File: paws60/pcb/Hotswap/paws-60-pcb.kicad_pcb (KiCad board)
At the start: 2 copper layers, 284.7 x 94.2 mm, 160 parts, among them J1 JST SH 4-pin, J2 AVR-ISP-6, SW1 Reset, U1 SRV05-4, U2 ATmega32U4-AU, Y1 16MHz

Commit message: Updated PCB for Paws60, remove ISO layout
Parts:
- removed the D45 at (38.7, 71.9)
- removed the MX44 at (251.9, 47.1)
- removed the MX46 at (273.3, 37.6)
- removed the MX47 at (11.4, 66.2)
- removed the MX49 at (32.8, 66.2)
- MX30: footprint MX_Only:MXOnly-1.5U-Hotswap-Rotated -> MX_Only:MXOnly-1.5U-Hotswap
- MX44: renamed from MX45; footprint MX_Only:MXOnly-2.25U-Hotswap-ReversedStabilizers-Left -> MX_Only:MXOnly-2.25U-Hotswap
- MX58: renamed from MX62; footprint MX_Only:MXOnly-2.75U-Hotswap -> MX_Only:MXOnly-2.75U-Hotswap-ReversedStabilizers
- moved D1 15.4 mm to (2.64, 3.98)
- moved D43 5.22 mm to (4.19, 67.3)
- moved J2 3.94 mm to (3.07, 20.3)
- moved R2 3.59 mm to (35.9, 16.4)
- moved C5 3.32 mm to (44.0, 32.3)
- moved Y1 3.30 mm to (44.0, 35.0)
- moved C7 3.28 mm to (44.0, 37.7)
- moved D42 2.52 mm to (244.9, 49.2)
- moved R1 2.32 mm to (34.7, 18.7)
- moved C2 2.29 mm to (14.9, 38.2)
- moved C4 2.23 mm to (21.8, 26.9)
- moved D3 1.91 mm to (36.8, 6.88)
- moved U2 1.77 mm to (26.8, 37.7)
- moved U1 1.73 mm to (40.1, 17.5)
- moved D2 0.74 mm to (19.6, 9.79)
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- renumbered D43 to D42, D44 to D43, D46 to D44, D47 to D45, D48 to D46, D49 to D47, D50 to D48, D51 to D49, D52 to D50, D53 to D51, D54 to D52, D55 to D53, D56 to D54, D57 to D55, D58 to D56, D59 to D57, D60 to D58, D61 to D59, D62 to D60, D63 to D61, D64 to D62, D65 to D63, MX48 to MX45, MX50 to MX46, MX51 to MX47, MX52 to MX48, MX53 to MX49, MX54 to MX50, MX55 to MX51, MX56 to MX52, MX57 to MX53, MX58 to MX54, MX59 to MX55, MX60 to MX56, MX61 to MX57, MX63 to MX59, MX64 to MX60, MX65 to MX61, MX66 to MX62, MX67 to MX63, MX68 to MX64, MX69 to MX65, MX70 to MX66, MX71 to MX67, MX72 to MX68, MX73 to MX69, MX74 to MX70, MX75 to MX71, MX76 to MX72, MX77 to MX73
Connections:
- D42 pad 2: Net-(D43-Pad2) (its old number) -> Net-(D42-Pad2)
- MX44 pad 1: Net-(D43-Pad2) (its old number) -> Net-(D42-Pad2)
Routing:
- net COL4: track 225.5 -> 298.4 mm, vias 5 -> 10
- net COL5: track 282.8 -> 350.6 mm, vias 5 -> 10
- net COL3: track 186.0 -> 245.5 mm, vias 5 -> 7
- net Net-(D43-Pad2): track 61.2 -> 10.5 mm
- net COL6: track 412.0 -> 459.1 mm, vias 9 -> 13
- net ROW2: track 349.0 -> 396.0 mm, vias 4 -> 6
- net Net-(D45-Pad2) (its old number): track 41.3 -> 0.00 mm, vias 4 -> 0
- net Net-(D42-Pad2): track 11.9 -> 48.2 mm
- net Net-(D43-Pad2) (its old number): track 30.2 -> 0.00 mm
- net COL7: track 396.2 -> 425.5 mm, vias 5 -> 10
- net ROW0: track 339.3 -> 366.4 mm
- net +5V: track 119.6 -> 142.6 mm, vias 6 -> 7
- net Net-(D2-Pad2): track 3.01 -> 20.6 mm
- net COL2: track 209.2 -> 226.5 mm, vias 13 -> 12
- net COL13: track 456.7 -> 440.6 mm, vias 12 -> 11
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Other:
- outline, holes or cut-outs redrawn

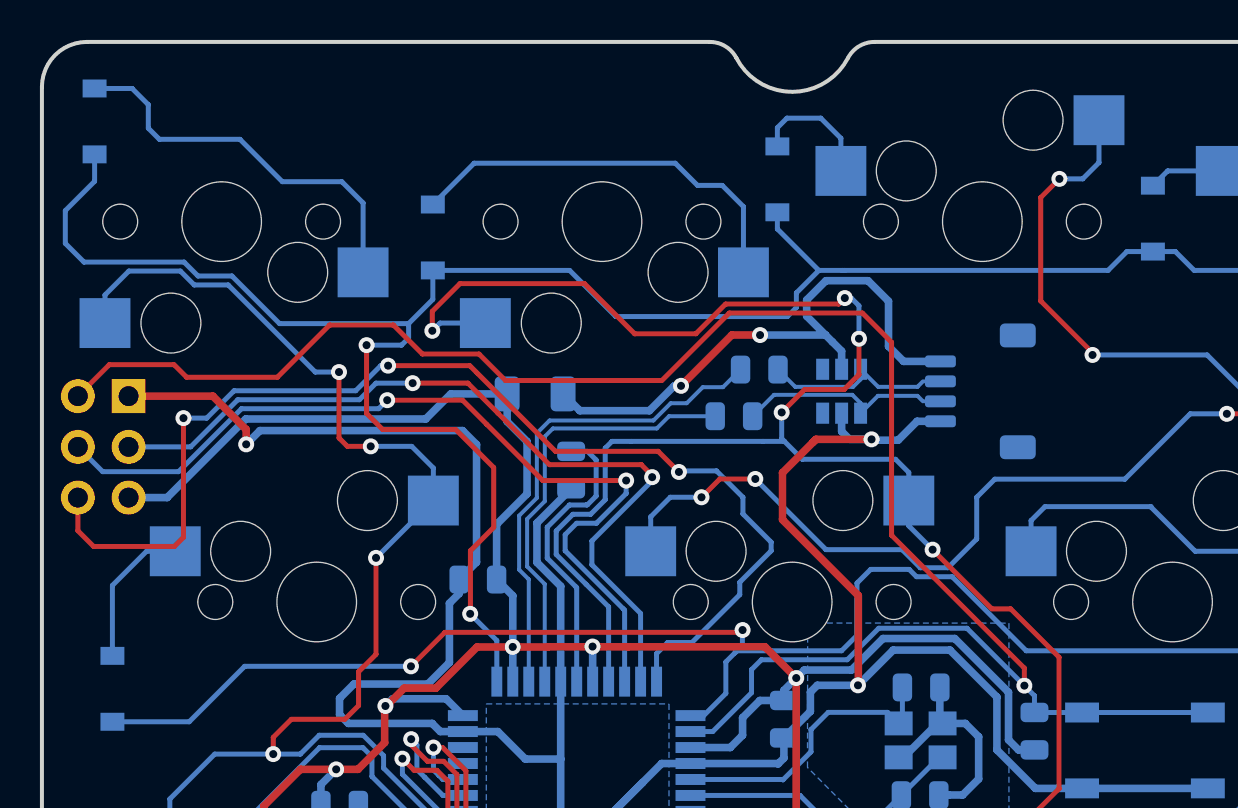
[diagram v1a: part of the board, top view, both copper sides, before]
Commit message: Added USB-C port, still not sure it correct or not
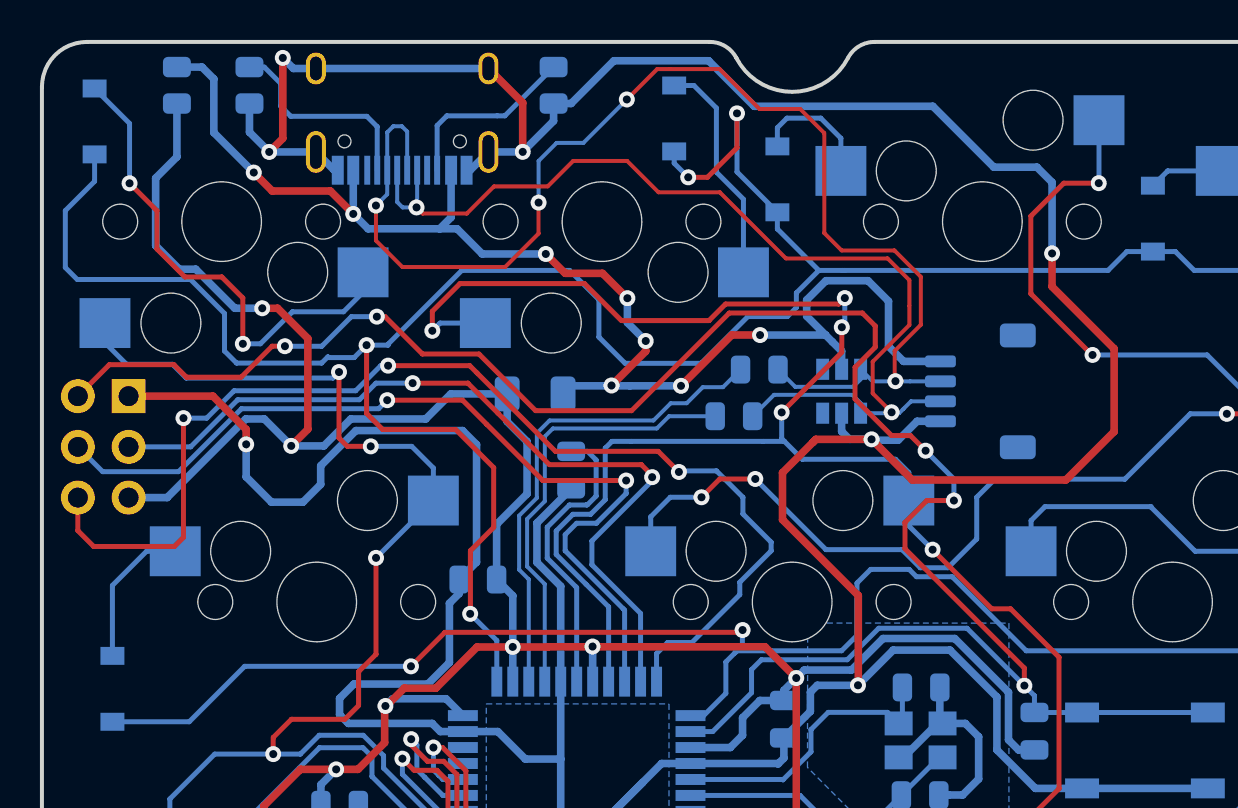
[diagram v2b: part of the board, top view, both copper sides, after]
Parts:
- added F2: Polyfuse, Resistor_SMD:R_0805_2012Metric, B.Cu at (6.76, 2.17)
- added R5: 5.1k, Resistor_SMD:R_0805_2012Metric, B.Cu at (10.4, 2.17)
- added R6: 5.1k, Resistor_SMD:R_0805_2012Metric, B.Cu at (25.6, 2.17)
- added USB1: HRO-TYPE-C-31-M-12, Type-C:HRO-TYPE-C-31-M-12, B.Cu at (18.0, -1.27)
- moved D2 13.5 mm to (31.7, 3.83)
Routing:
- net GND: track 181.1 -> 274.4 mm, vias 5 -> 9
- net D-: track 9.63 -> 65.3 mm, vias 0 -> 4
- net D+: track 11.0 -> 51.5 mm, vias 0 -> 2
- net VBUS: track 29.4 -> 68.4 mm, vias 2 -> 8
- net +5V: track 142.6 -> 166.6 mm, vias 7 -> 9
- net ROW0: track 366.4 -> 381.2 mm, vias 6 -> 8
- net Net-(R5-Pad1): track 0.00 -> 10.5 mm
- net Net-(R6-Pad1): track 0.00 -> 9.28 mm
- net Net-(D2-Pad2): track 20.6 -> 11.4 mm
- net RST: track 96.8 -> 102.7 mm, vias 1 -> 5
- net Net-(D1-Pad2): track 20.0 -> 25.0 mm, vias 0 -> 2
- net COL1: track 205.6 -> 203.2 mm
- net COL0: track 199.7 -> 197.5 mm
- net COL2: track 226.5 -> 227.2 mm
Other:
- board text added: "Paws 60 v1.0"
- board text removed: "Bakeneko 60 v3.0"

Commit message: Move crystal more closer to MCU, ya yeet
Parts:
- moved Y1 5.39 mm to (38.8, 36.5)
- moved C5 5.39 mm to (38.9, 33.8)
- moved C7 5.35 mm to (38.8, 39.2)
- moved C1 1.56 mm to (35.6, 33.7)
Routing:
- net XTAL2: track 14.6 -> 7.71 mm
- net XTAL1: track 14.5 -> 8.83 mm
- net Net-(D17-Pad2): track 48.9 -> 47.6 mm
- net RST: track 102.7 -> 103.5 mm
- net +5V: track 166.6 -> 167.3 mm
- net GND: track 274.4 -> 274.0 mm, vias 9 -> 11

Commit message: Re-wire, ...
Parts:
- removed the D42 at (244.9, 49.2)
- MX58: footprint MX_Only:MXOnly-2.75U-Hotswap-ReversedStabilizers -> MX_Only:MXOnly-2.75U-Hotswap
- moved D20 13.9 mm to (86.3, 16.1)
- moved D55 10.6 mm to (282.5, 61.0)
- moved D29 2.60 mm to (258.6, 28.8)
- moved D63 1.52 mm to (261.3, 87.5)
- moved D62 1.38 mm to (237.5, 87.4)
- moved D17 0.67 mm to (67.3, 16.1)
- moved F1 0.54 mm to (24.2, 17.6)
- moved C6 0.46 mm to (26.0, 21.4)
- moved C5 0.43 mm to (38.9, 33.4)
- moved Y1 0.42 mm to (38.8, 36.1)
- moved C7 0.38 mm to (38.8, 38.8)
- turned MX56 to 180 degrees
- turned MX57 to 180 degrees
- turned MX58 to 0 degrees
- turned MX64 to 180 degrees
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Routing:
- net COL13: track 440.6 -> 402.0 mm, vias 11 -> 8
- net Net-(D55-Pad2): track 22.3 -> 47.9 mm
- net ROW3: track 353.0 -> 374.9 mm, vias 4 -> 6
- net Net-(D42-Pad2): track 48.2 -> 30.4 mm
- net ROW2: track 396.0 -> 379.9 mm, vias 6 -> 4
- net Net-(D54-Pad2): track 6.96 -> 22.1 mm
- net Net-(D20-Pad2): track 3.17 -> 15.2 mm, vias 0 -> 2
- net ROW1: track 324.4 -> 314.7 mm, vias 2 -> 4
- net ROW4: track 374.4 -> 365.2 mm
- net COL3: track 245.5 -> 236.3 mm
- net COL1: track 203.2 -> 195.1 mm, vias 12 -> 10
- net GND: track 274.0 -> 266.1 mm
- net ROW0: track 381.2 -> 374.9 mm
- net COL4: track 298.4 -> 292.2 mm
- net COL5: track 350.6 -> 344.6 mm
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
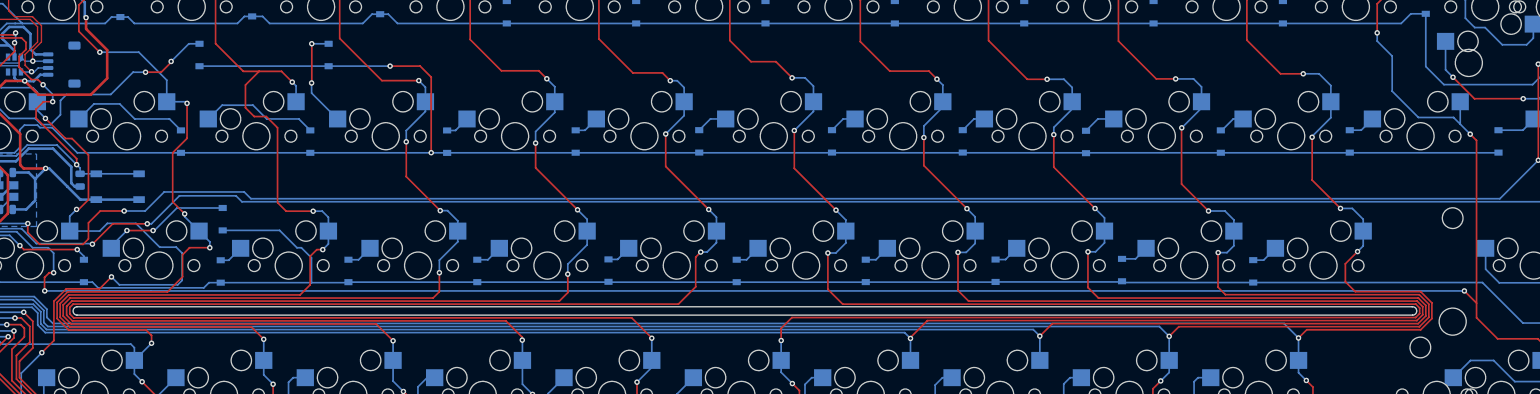
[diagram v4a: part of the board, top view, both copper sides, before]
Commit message: Move diode out, since it was accident block JST port
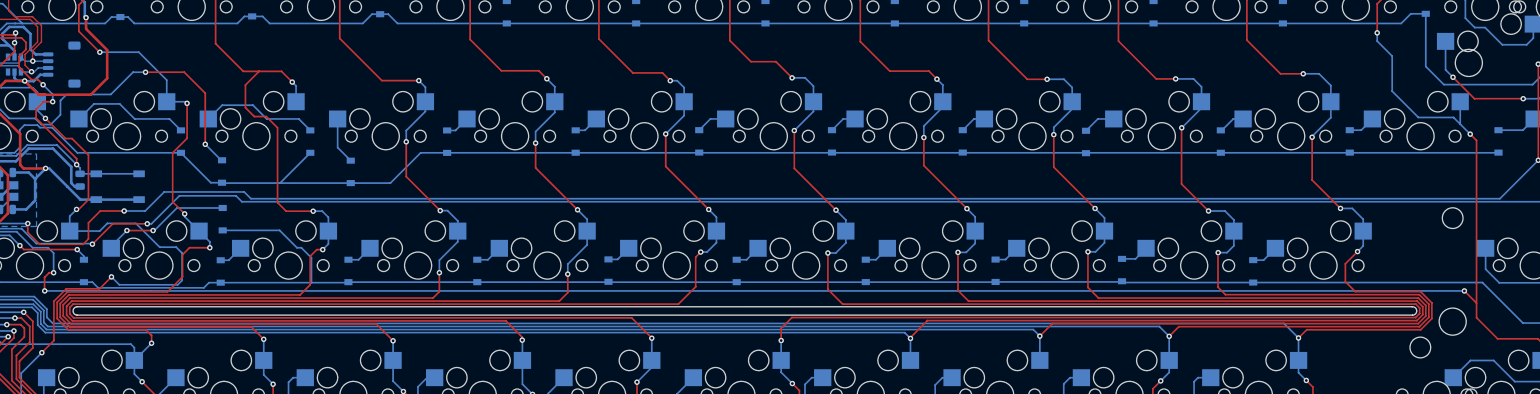
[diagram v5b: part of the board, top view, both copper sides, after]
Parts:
- moved D20 17.5 mm to (89.6, 33.3)
- moved D17 17.5 mm to (70.6, 33.2)
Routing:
- net ROW1: track 314.7 -> 278.7 mm, vias 4 -> 2
- net Net-(D17-Pad2): track 47.3 -> 58.7 mm
- net Net-(D20-Pad2): track 15.2 -> 6.94 mm, vias 2 -> 0
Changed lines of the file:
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@@
   )
   (footprint "Diode_SMD:D_SOD-123" (layer "B.Cu")
-    (at 67.290028 16.087692 90)
+    (at 70.614414 33.244321 90)
     (descr "SOD-123")
     (tags "SOD-123")
@@
   )
   (footprint "Diode_SMD:D_SOD-123" (layer "B.Cu")
-    (at 86.309883 16.087692 90)
+    (at 89.572531 33.301911 90)
     (descr "SOD-123")
     (tags "SOD-123")
@@
   (segment (start 3.530355 27.220074) (end 3.530355 30.749098) (width 0.25) (layer "B.Cu") (net 20))
   (segment (start 6.6775 25.51) (end 5.240429 25.51) (width 0.25) (layer "B.Cu") (net 20))
-  (segment (start 59.346744 18.625704) (end 61.656169 18.625704) (width 0.25) (layer "F.Cu") (net 21))
+  (segment (start 65.056628 18.625704) (end 68.142143 21.711219) (width 0.25) (layer "F.Cu") (net 21))
   (segment (start 33.033815 22.804311) (end 33.95009 21.888036) (width 0.25) (layer "F.Cu") (net 21))
-  (segment (start 61.656169 18.625704) (end 63.152415 17.129458) (width 0.25) (layer "F.Cu") (net 21))
+  (segment (start 59.346744 18.625704) (end 65.056628 18.625704) (width 0.25) (layer "F.Cu") (net 21))
+  (segment (start 68.142143 21.711219) (end 68.142143 29.236315) (width 0.25) (layer "F.Cu") (net 21))
   (segment (start 33.95009 21.888036) (end 35.728742 21.888036) (width 0.25) (layer "F.Cu") (net 21))
   (via (at 35.728742 21.888036) (size 0.8) (drill 0.4) (layers "F.Cu" "B.Cu") (net 21))
+  (via (at 68.142143 29.236315) (size 0.8) (drill 0.4) (layers "F.Cu" "B.Cu") (net 21))
   (via (at 33.033815 22.804311) (size 0.8) (drill 0.4) (layers "F.Cu" "B.Cu") (net 21))
   (via (at 59.346744 18.625704) (size 0.8) (drill 0.4) (layers "F.Cu" "B.Cu") (net 21))
-  (via (at 63.117264 17.03842) (size 0.8) (drill 0.4) (layers "F.Cu" "B.Cu") (net 21))
   (segment (start 54.237506 21.898925) (end 57.510727 18.625704) (width 0.25) (layer "B.Cu") (net 21))
   (segment (start 35.728742 21.888036) (end 39.268713 25.428007) (width 0.25) (layer "B.Cu") (net 21))
   (segment (start 43.081174 25.428007) (end 43.987833 26.334666) (width 0.25) (layer "B.Cu") (net 21))
   (segment (start 30.49 25.51) (end 30.49 23.785068) (width 0.25) (layer "B.Cu") (net 21))
+  (segment (start 70.500149 31.594321) (end 68.142143 29.236315) (width 0.25) (layer "B.Cu") (net 21))
   (segment (start 31.470757 22.804311) (end 33.033815 22.804311) (width 0.25) (layer "B.Cu") (net 21))
   (segment (start 30.49 23.785068) (end 31.470757 22.804311) (width 0.25) (layer "B.Cu") (net 21))
   (segment (start 39.268713 25.428007) (end 43.081174 25.428007) (width 0.25) (layer "B.Cu") (net 21))
-  (segment (start 67.290028 14.437692) (end 65.717992 14.437692) (width 0.25) (layer "B.Cu") (net 21))
+  (segment (start 70.614414 31.594321) (end 70.500149 31.594321) (width 0.25) (layer "B.Cu") (net 21))
   (segment (start 47.722677 21.898925) (end 54.237506 21.898925) (width 0.25) (layer "B.Cu") (net 21))
-  (segment (start 65.717992 14.437692) (end 63.117264 17.03842) (width 0.25) (layer "B.Cu") (net 21))
   (segment (start 46.817291 22.804311) (end 47.722677 21.898925) (width 0.25) (layer "B.Cu") (net 21))
   (segment (start 43.987833 26.334666) (end 45.376583 26.334666) (width 0.25) (layer "B.Cu") (net 21))
@@
   (segment (start 46.817291 24.893958) (end 46.817291 22.804311) (width 0.25) (layer "B.Cu") (net 21))
   (segment (start 45.376583 26.334666) (end 46.817291 24.893958) (width 0.25) (layer "B.Cu") (net 21))
-  (segment (start 99.798033 17.724283) (end 95.365912 17.724283) (width 0.25) (layer "F.Cu") (net 22))
   (segment (start 20.184579 29.57) (end 34.976335 29.57) (width 0.25) (layer "F.Cu") (net 22))
-  (segment (start 101.421837 30.48) (end 101.421837 19.348087) (width 0.25) (layer "F.Cu") (net 22))
-  (segment (start 101.421837 19.348087) (end 99.798033 17.724283) (width 0.25) (layer "F.Cu") (net 22))
   (segment (start 34.976335 29.57) (end 35.091728 29.454607) (width 0.25) (layer "F.Cu") (net 22))
   (segment (start 18.48296 31.271619) (end 20.184579 29.57) (width 0.25) (layer "F.Cu") (net 22))
   (via (at 35.091728 29.454607) (size 0.8) (drill 0.4) (layers "F.Cu" "B.Cu") (net 22))
   (via (at 18.48296 31.271619) (size 0.8) (drill 0.4) (layers "F.Cu" "B.Cu") (net 22))
-  (via (at 101.421837 30.48) (size 0.8) (drill 0.4) (layers "F.Cu" "B.Cu") (net 22))
-  (via (at 95.365912 17.724283) (size 0.8) (drill 0.4) (layers "F.Cu" "B.Cu") (net 22))
   (segment (start 3.530355 34.049098) (end 7.377436 34.049098) (width 0.25) (layer "B.Cu") (net 22))
   (segment (start 43.801636 26.784186) (end 43.434954 26.417505) (width 0.25) (layer "B.Cu") (net 22))
   (segment (start 40.821567 29.722973) (end 40.05079 30.49375) (width 0.25) (layer "B.Cu") (net 22))
   (segment (start 10.154915 31.271619) (end 10.139034 31.2875) (width 0.25) (layer "B.Cu") (net 22))
+  (segment (start 89.572531 34.951911) (end 70.672004 34.951911) (width 0.25) (layer "B.Cu") (net 22))
   (segment (start 32.482533 33.739519) (end 32.482533 31.282609) (width 0.25) (layer "B.Cu") (net 22))
   (segment (start 18.48296 31.271619) (end 10.154915 31.271619) (width 0.25) (layer "B.Cu") (net 22))
+  (segment (start 79.211929 34.894321) (end 83.6125 30.49375) (width 0.25) (layer "B.Cu") (net 22))
+  (segment (start 68.963071 34.894321) (end 64.5625 30.49375) (width 0.25) (layer "B.Cu") (net 22))
   (segment (start 45.588288 26.784186) (end 43.801636 26.784186) (width 0.25) (layer "B.Cu") (net 22))
-  (segment (start 67.28452 17.724283) (end 95.365912 17.724283) (width 0.25) (layer "B.Cu") (net 22))
+  (segment (start 258.59 30.49375) (end 99.8675 30.49375) (width 0.25) (layer "B.Cu") (net 22))
   (segment (start 32.482533 31.282609) (end 33.271392 30.49375) (width 0.25) (layer "B.Cu") (net 22))
   (segment (start 43.434954 26.417505) (end 41.506682 26.417505) (width 0.25) (layer "B.Cu") (net 22))
+  (segment (start 70.672004 34.951911) (end 70.614414 34.894321) (width 0.25) (layer "B.Cu") (net 22))
+  (segment (start 70.614414 34.894321) (end 68.963071 34.894321) (width 0.25) (layer "B.Cu") (net 22))
   (segment (start 7.377436 34.049098) (end 10.139034 31.2875) (width 0.25) (layer "B.Cu") (net 22))
   (segment (start 40.821567 27.10262) (end 40.821567 29.722973) (width 0.25) (layer "B.Cu") (net 22))
   (segment (start 33.271392 30.49375) (end 40.05079 30.49375) (width 0.25) (layer "B.Cu") (net 22))
+  (segment (start 95.409339 34.951911) (end 89.572531 34.951911) (width 0.25) (layer "B.Cu") (net 22))
   (segment (start 41.506682 26.417505) (end 40.821567 27.10262) (width 0.25) (layer "B.Cu") (net 22))
   (segment (start 35.091728 29.454607) (end 36.130871 30.49375) (width 0.25) (layer "B.Cu") (net 22))
   (segment (start 64.5625 30.49375) (end 49.297852 30.49375) (width 0.25) (layer "B.Cu") (net 22))
-  (segment (start 64.5625 30.49375) (end 258.59 30.49375) (width 0.25) (layer "B.Cu") (net 22))
   (segment (start 49.297852 30.49375) (end 45.588288 26.784186) (width 0.25) (layer "B.Cu") (net 22))
+  (segment (start 99.8675 30.49375) (end 95.409339 34.951911) (width 0.25) (layer "B.Cu") (net 22))
   (segment (start 57.760431 25.51) (end 55.546036 23.295605) (width 0.25) (layer "B.Cu") (net 23))
   (segment (start 62.87875 25.51) (end 57.760431 25.51) (width 0.25) (layer "B.Cu") (net 23))
@@
   (segment (start 77.199888 25.51) (end 81.92875 25.51) (width 0.25) (layer "B.Cu") (net 24))
   (segment (start 70.634883 23.482027) (end 75.171914 23.482027) (width 0.25) (layer "B.Cu") (net 24))
-  (segment (start 83.829426 14.430104) (end 83.829426 20.183741) (width 0.25) (layer "F.Cu") (net 25))
-  (segment (start 83.829426 20.183741) (end 83.803854 20.209313) (width 0.25) (layer "F.Cu") (net 25))
-  (via (at 83.829426 14.430104) (size 0.8) (drill 0.4) (layers "F.Cu" "B.Cu") (net 25))
-  (via (at 83.803854 20.209313) (size 0.8) (drill 0.4) (layers "F.Cu" "B.Cu") (net 25))
-  (segment (start 86.309883 14.437692) (end 83.800839 14.437692) (width 0.25) (layer "B.Cu") (net 25))
-  (segment (start 87.64 25.51) (end 87.615 25.51) (width 0.25) (layer "B.Cu") (net 25))
-  (segment (start 83.803854 21.698854) (end 87.615 25.51) (width 0.25) (layer "B.Cu") (net 25))
-  (segment (start 83.803854 21.698854) (end 83.803854 20.209313) (width 0.25) (layer "B.Cu") (net 25))
+  (segment (start 87.64 29.71938) (end 89.572531 31.651911) (width 0.25) (layer "B.Cu") (net 25))
+  (segment (start 87.64 25.51) (end 87.64 29.71938) (width 0.25) (layer "B.Cu") (net 25))
   (segment (start 106.69 25.51) (end 104.996356 27.203644) (width 0.25) (layer "B.Cu") (net 26))
   (segment (start 104.996356 27.203644) (end 103.764217 27.203644) (width 0.25) (layer "B.Cu") (net 26))
@@
   (segment (start 29.4447 20.005892) (end 37.187134 20.005892) (width 0.25) (layer "B.Cu") (net 77))
   (segment (start 43.417 22.97) (end 43.417 24.23787) (width 0.25) (layer "B.Cu") (net 77))
-  (segment (start 44.078163 59.925836) (end 44.037467 59.925836) (width 0.25) (layer "B.Cu") (net 77))
   (segment (start 38.082944 20.901702) (end 42.752539 20.901702) (width 0.25) (layer "B.Cu") (net 77))
   (segment (start 27.607626 28.472984) (end 27.607626 24.008039) (width 0.25) (layer "B.Cu") (net 77))

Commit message: Change new mount, blah blah...
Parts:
- added S1: Screw, Type-C:10x5_7x2.5mm, F.Cu at (1.86, 56.6)
- added S2: Screw, Type-C:10x5_7x2.5mm, F.Cu at (282.8, 56.6)
- moved D55 15.2 mm to (282.8, 76.2)
- moved J2 13.6 mm to (3.05, 33.9)
- moved D16 9.73 mm to (1.97, 22.8)
- moved D42 4.90 mm to (281.5, 49.8)
- moved R5 4.34 mm to (6.13, 2.97), turned to 0 degrees
- moved F2 3.00 mm to (6.93, 5.16), turned to 0 degrees
- moved R3 1.10 mm to (27.3, 56.4)
- moved D45 0.78 mm to (61.8, 68.6)
- moved C3 0.69 mm to (31.7, 46.9)
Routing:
- net COL7: track 421.5 -> 386.9 mm, vias 10 -> 6
- net COL4: track 292.2 -> 259.4 mm, vias 10 -> 6
- net COL5: track 344.6 -> 315.2 mm, vias 10 -> 6
- net COL3: track 236.3 -> 212.9 mm, vias 7 -> 5
- net SCK: track 42.4 -> 64.9 mm
- net ROW3: track 374.9 -> 355.8 mm, vias 6 -> 4
- net MOSI: track 40.4 -> 56.5 mm, vias 2 -> 4
- net MISO: track 56.0 -> 71.2 mm
- net RST: track 103.0 -> 116.6 mm
- net ROW4: track 365.2 -> 378.8 mm, vias 6 -> 8
- net COL0: track 191.5 -> 181.9 mm, vias 10 -> 11
- net COL6: track 453.9 -> 444.5 mm, vias 13 -> 10
- net GND: track 266.1 -> 273.5 mm, vias 11 -> 10
- net ROW2: track 379.9 -> 373.7 mm
- net Net-(R5-Pad1): track 10.5 -> 16.6 mm, vias 0 -> 2
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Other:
- outline, holes or cut-outs redrawn
